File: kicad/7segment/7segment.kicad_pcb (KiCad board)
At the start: 2 copper layers, 49.5 x 30.5 mm, 11 parts, among them P1 CONN_01X05, U1 74HC595

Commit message: Add a nice logo
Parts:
- added G***: made by ami, led2layer:superme, F.Cu at (113.8, 102.1)
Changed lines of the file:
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@@
     (tracks 107)
     (zones 0)
-    (modules 11)
+    (modules 12)
     (nets 23)
   )
@@
     (pad_to_mask_clearance 0.2)
     (aux_axis_origin 0 0)
+    (grid_origin 105.156 73.914)
     (visible_elements 7FFFFFFF)
     (pcbplotparams
@@
     )
   )
+  (module led2layer:superme (layer F.Cu)
+    (at 113.792 102.108)
+    (fp_text reference G*** (at 0 0) (layer F.SilkS) hide
+      (effects (font (thickness 0.3)))
+    )
+    (fp_text value "made by ami" (at 11.938 1.524) (layer F.SilkS)
+      (effects (font (thickness 0.3)))
+    )
+    (fp_poly (pts (xy -1.174848 -1.001932) (xy -1.108553 -0.835263) (xy -1.101964 -0.783166) (xy -1.154454 -0.687075)
+      (xy -1.261268 -0.703585) (xy -1.307612 -0.754359) (xy -1.321651 -0.891512) (xy -1.300826 -0.973125)
+      (xy -1.241858 -1.063868) (xy -1.174848 -1.001932)) (layer F.SilkS) (width 0.01))
+    (fp_poly (pts (xy -1.354667 -0.635) (xy -1.397 -0.592666) (xy -1.439334 -0.635) (xy -1.397 -0.677333)
+      (xy -1.354667 -0.635)) (layer F.SilkS) (width 0.01))
+    (fp_poly (pts (xy -1.222468 -0.515682) (xy -1.213556 -0.461942) (xy -1.232025 -0.346905) (xy -1.293325 -0.393625)
+      (xy -1.308718 -0.417483) (xy -1.304455 -0.524221) (xy -1.285493 -0.540758) (xy -1.222468 -0.515682)) (layer F.SilkS) (width 0.01))
+    (fp_poly (pts (xy 0.599715 -2.134372) (xy 0.911081 -2.038929) (xy 1.037166 -1.989426) (xy 1.167461 -1.881387)
+      (xy 1.162036 -1.761872) (xy 1.029634 -1.692658) (xy 0.994833 -1.690333) (xy 0.868566 -1.682959)
+      (xy 0.880286 -1.647657) (xy 1.016 -1.566333) (xy 1.137143 -1.47808) (xy 1.103782 -1.442679)
+      (xy 1.095464 -1.442333) (xy 0.94105 -1.385676) (xy 0.776868 -1.26568) (xy 0.623349 -1.156396)
+      (xy 0.516497 -1.137748) (xy 0.409623 -1.120328) (xy 0.337892 -1.057401) (xy 0.276273 -0.955299)
+      (xy 0.288945 -0.931333) (xy 0.297454 -0.868359) (xy 0.24551 -0.740833) (xy 0.194676 -0.622351)
+      (xy 0.213574 -0.613099) (xy 0.325194 -0.619887) (xy 0.415543 -0.570765) (xy 0.505205 -0.50776)
+      (xy 0.476141 -0.560746) (xy 0.4515 -0.592907) (xy 0.398848 -0.731912) (xy 0.471792 -0.883059)
+      (xy 0.591547 -0.994178) (xy 0.669689 -0.941895) (xy 0.707091 -0.725624) (xy 0.707114 -0.725223)
+      (xy 0.75408 -0.563375) (xy 0.831881 -0.50806) (xy 0.913935 -0.581838) (xy 0.925563 -0.740833)
+      (xy 0.934117 -0.971933) (xy 0.970574 -1.121833) (xy 1.09131 -1.239379) (xy 1.260868 -1.266013)
+      (xy 1.394579 -1.189125) (xy 1.397 -1.185333) (xy 1.367024 -1.122551) (xy 1.232663 -1.100666)
+      (xy 1.071188 -1.071386) (xy 1.016 -1.013272) (xy 1.085663 -0.923804) (xy 1.239987 -0.84161)
+      (xy 1.396976 -0.803943) (xy 1.45309 -0.814692) (xy 1.487392 -0.774007) (xy 1.481946 -0.620595)
+      (xy 1.441314 -0.40516) (xy 1.404521 -0.275166) (xy 1.325172 -0.117043) (xy 1.219304 -0.110291)
+      (xy 1.059049 -0.253209) (xy 1.058333 -0.254) (xy 0.896313 -0.383263) (xy 0.75405 -0.420317)
+      (xy 0.679782 -0.355588) (xy 0.677333 -0.329608) (xy 0.615403 -0.273913) (xy 0.545935 -0.286305)
+      (xy 0.458536 -0.292222) (xy 0.466266 -0.25303) (xy 0.429348 -0.196794) (xy 0.25794 -0.170137)
+      (xy 0.211666 -0.169333) (xy 0.009146 -0.148731) (xy -0.044548 -0.090596) (xy -0.03927 -0.07971)
+      (xy 0.077479 -0.030202) (xy 0.259994 -0.04365) (xy 0.461311 -0.06376) (xy 0.600186 -0.038595)
+      (xy 0.644412 0.013937) (xy 0.561786 0.075929) (xy 0.507146 0.093778) (xy 0.381749 0.13362)
+      (xy 0.403153 0.152254) (xy 0.574157 0.160894) (xy 0.804189 0.128672) (xy 0.900715 0.042334)
+      (xy 0.991026 -0.075065) (xy 1.075142 -0.043102) (xy 1.100666 0.0743) (xy 1.047241 0.246943)
+      (xy 0.924174 0.370553) (xy 0.787281 0.393643) (xy 0.765708 0.383292) (xy 0.695404 0.40585)
+      (xy 0.677333 0.503003) (xy 0.643188 0.626095) (xy 0.510212 0.672918) (xy 0.402166 0.676812)
+      (xy 0.121918 0.635573) (xy -0.127 0.546757) (xy -0.353951 0.391646) (xy -0.576503 0.181687)
+      (xy -0.602339 0.151756) (xy -0.731681 -0.017739) (xy -0.780609 -0.157721) (xy -0.761236 -0.340022)
+      (xy -0.726476 -0.479778) (xy 0.197555 -0.479778) (xy 0.209177 -0.429443) (xy 0.254 -0.423333)
+      (xy 0.32369 -0.454311) (xy 0.310444 -0.479778) (xy 0.209964 -0.489911) (xy 0.197555 -0.479778)
+      (xy -0.726476 -0.479778) (xy -0.715968 -0.522022) (xy -0.660159 -0.792024) (xy -0.640938 -1.01317)
+      (xy -0.64793 -1.082036) (xy -0.62543 -1.204114) (xy -0.386331 -1.204114) (xy -0.381486 -1.186119)
+      (xy -0.270983 -1.135403) (xy -0.061435 -1.114251) (xy 0.001014 -1.115195) (xy 0.198078 -1.138974)
+      (xy 0.289154 -1.182671) (xy 0.287839 -1.199076) (xy 0.182833 -1.244031) (xy -0.02455 -1.268502)
+      (xy -0.094661 -1.27) (xy -0.305222 -1.252056) (xy -0.386331 -1.204114) (xy -0.62543 -1.204114)
+      (xy -0.623635 -1.21385) (xy -0.460956 -1.339383) (xy -0.382569 -1.379201) (xy -0.167508 -1.467551)
+      (xy -0.013347 -1.473249) (xy 0.165174 -1.399149) (xy 0.168093 -1.397641) (xy 0.35354 -1.329977)
+      (xy 0.459959 -1.345811) (xy 0.462091 -1.348881) (xy 0.436878 -1.434438) (xy 0.361062 -1.475443)
+      (xy 0.215341 -1.584564) (xy 0.170875 -1.651) (xy 0.508 -1.651) (xy 0.550333 -1.608666)
+      (xy 0.592666 -1.651) (xy 0.550333 -1.693333) (xy 0.508 -1.651) (xy 0.170875 -1.651)
+      (xy 0.112621 -1.738035) (xy 0.059154 -1.907252) (xy 0.121908 -2.017901) (xy 0.201843 -2.075683)
+      (xy 0.377058 -2.145203) (xy 0.599715 -2.134372)) (layer F.SilkS) (width 0.01))
+    (fp_poly (pts (xy -0.638427 0.696059) (xy -0.610657 0.710364) (xy -0.333584 0.806884) (xy -0.041216 0.846667)
+      (xy 0.165659 0.864221) (xy 0.244082 0.930096) (xy 0.246309 0.994834) (xy 0.262332 1.209076)
+      (xy 0.348042 1.354723) (xy 0.473778 1.382126) (xy 0.476974 1.380945) (xy 0.557863 1.379531)
+      (xy 0.562261 1.490911) (xy 0.544479 1.576791) (xy 0.458654 1.791871) (xy 0.354662 1.926167)
+      (xy 0.162109 1.999354) (xy -0.12816 2.025034) (xy -0.45155 2.003951) (xy -0.743462 1.936849)
+      (xy -0.804334 1.912802) (xy -1.037774 1.776617) (xy -1.27972 1.589056) (xy -1.312334 1.559029)
+      (xy -1.462258 1.403416) (xy -1.492103 1.322867) (xy -1.422145 1.288472) (xy -1.272339 1.190234)
+      (xy -1.230246 1.116392) (xy -1.144008 0.944686) (xy -1.028387 0.773864) (xy -0.914312 0.645319)
+      (xy -0.808973 0.623131) (xy -0.638427 0.696059)) (layer F.SilkS) (width 0.01))
+    (fp_poly (pts (xy -0.123116 2.973568) (xy -0.112531 3.02262) (xy -0.122531 3.040769) (xy -0.10438 3.132843)
+      (xy -0.064028 3.156069) (xy -0.075412 3.175931) (xy -0.220909 3.185308) (xy -0.359317 3.184467)
+      (xy -0.59383 3.168927) (xy -0.738789 3.140046) (xy -0.761484 3.122084) (xy -0.688705 3.071024)
+      (xy -0.511422 3.019125) (xy -0.497417 3.01625) (xy -0.242246 2.972044) (xy -0.123116 2.973568)) (layer F.SilkS) (width 0.01))
+    (fp_poly (pts (xy -1.100667 3.175) (xy -1.143 3.217334) (xy -1.185334 3.175) (xy -1.143 3.132667)
+      (xy -1.100667 3.175)) (layer F.SilkS) (width 0.01))
+    (fp_poly (pts (xy -1.439334 3.175) (xy -1.481667 3.217334) (xy -1.524 3.175) (xy -1.481667 3.132667)
+      (xy -1.439334 3.175)) (layer F.SilkS) (width 0.01))
+    (fp_poly (pts (xy 4.318 3.386667) (xy -0.014112 3.386667) (xy -0.85098 3.385848) (xy -1.632976 3.383496)
+      (xy -2.344464 3.37977) (xy -2.969807 3.374827) (xy -3.493371 3.368825) (xy -3.899518 3.361923)
+      (xy -4.172613 3.354279) (xy -4.297021 3.34605) (xy -4.302872 3.343316) (xy -4.211925 3.334447)
+      (xy -3.968661 3.326199) (xy -3.590095 3.318758) (xy -3.093242 3.312313) (xy -2.495118 3.307049)
+      (xy -1.812737 3.303156) (xy -1.063115 3.30082) (xy -0.388637 3.300199) (xy 3.482246 3.300432)
+      (xy 3.426447 3.124624) (xy 3.33836 2.921254) (xy 3.19991 2.674949) (xy 3.040775 2.430322)
+      (xy 2.890634 2.231989) (xy 2.779164 2.124563) (xy 2.755944 2.116667) (xy 2.615922 2.062118)
+      (xy 2.553992 2.012126) (xy 2.424906 1.938697) (xy 2.181789 1.842314) (xy 1.874531 1.742508)
+      (xy 1.838558 1.732044) (xy 1.527171 1.638355) (xy 1.346147 1.564754) (xy 1.262095 1.488226)
+      (xy 1.241621 1.385758) (xy 1.244432 1.322552) (xy 1.311817 1.119249) (xy 1.464825 0.873366)
+      (xy 1.556956 0.76123) (xy 1.75631 0.493924) (xy 1.914345 0.201321) (xy 1.955278 0.091535)
+      (xy 2.051101 -0.132736) (xy 2.165889 -0.277111) (xy 2.200698 -0.296132) (xy 2.379044 -0.439029)
+      (xy 2.538287 -0.746089) (xy 2.622211 -1.002439) (xy 2.656289 -1.272941) (xy 2.5907 -1.566551)
+      (xy 2.564276 -1.637439) (xy 2.402392 -1.96713) (xy 2.189727 -2.287811) (xy 1.962933 -2.551272)
+      (xy 1.758662 -2.709306) (xy 1.744278 -2.716) (xy 1.540879 -2.817728) (xy 1.439333 -2.878515)
+      (xy 1.264743 -2.970376) (xy 1.081117 -3.04534) (xy 0.91349 -3.145121) (xy 0.899675 -3.256956)
+      (xy 0.938361 -3.301971) (xy 1.029329 -3.335469) (xy 1.194012 -3.359052) (xy 1.453843 -3.374324)
+      (xy 1.830254 -3.382888) (xy 2.344679 -3.386348) (xy 2.633725 -3.386666) (xy 4.318 -3.386666)
+      (xy 4.318 3.386667)) (layer F.SilkS) (width 0.01))
+  )
   (gr_text "(C) Amitesh Singh 2017" (at 136.652 91.694 90) (layer B.SilkS)
     (effects (font (size 1.5 1.5) (thickness 0.3)) (justify mirror))
@@
     (effects (font (size 1.5 1.5) (thickness 0.3) italic))
   )
-  (gr_text V0.1 (at 113.284 104.14) (layer F.SilkS)
+  (gr_text V0.1 (at 154.178 78.486) (layer F.SilkS)
     (effects (font (size 1.5 1.5) (thickness 0.3)))
   )

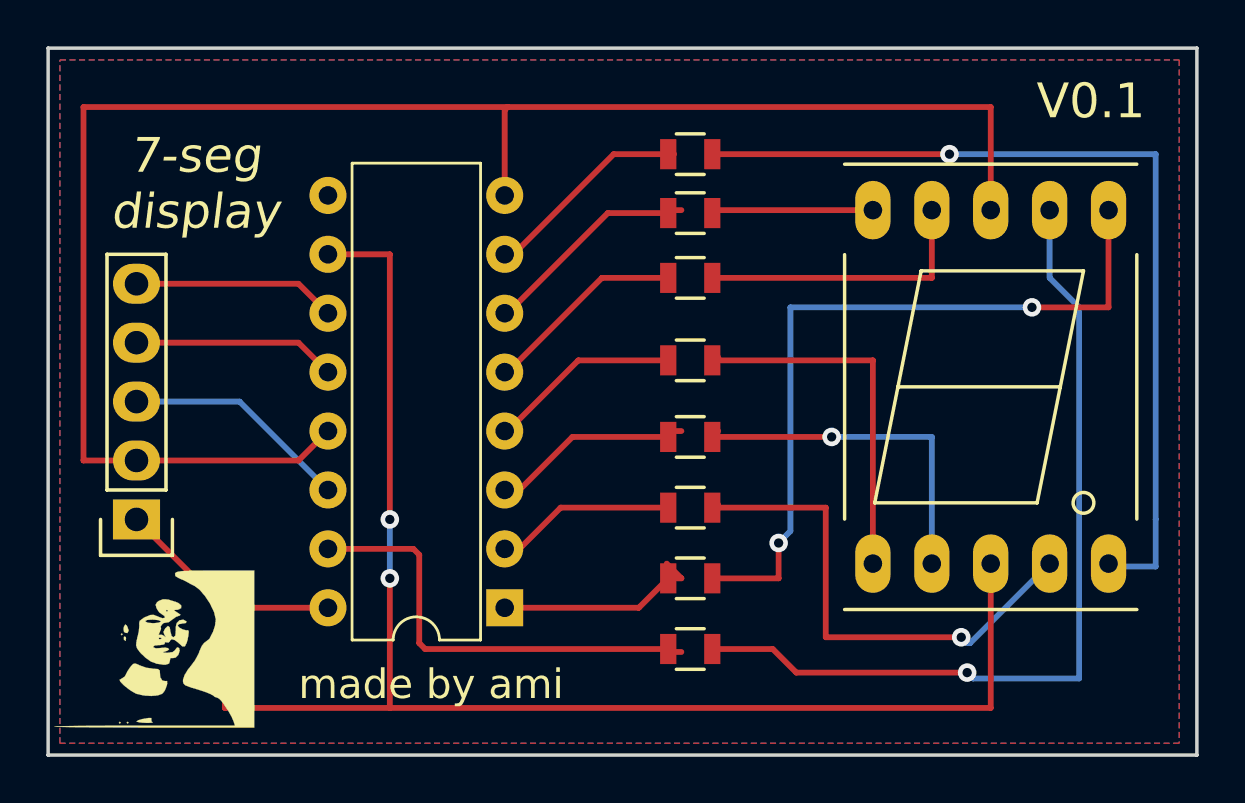
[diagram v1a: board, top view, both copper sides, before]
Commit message: update the 7segment a bit
mistakes corrected.

- remove right angled traces
- minimize the vias
- add a 2.0 mm hole

Signed-off-by: Amitesh Singh <singh.amitesh@gmail.com>
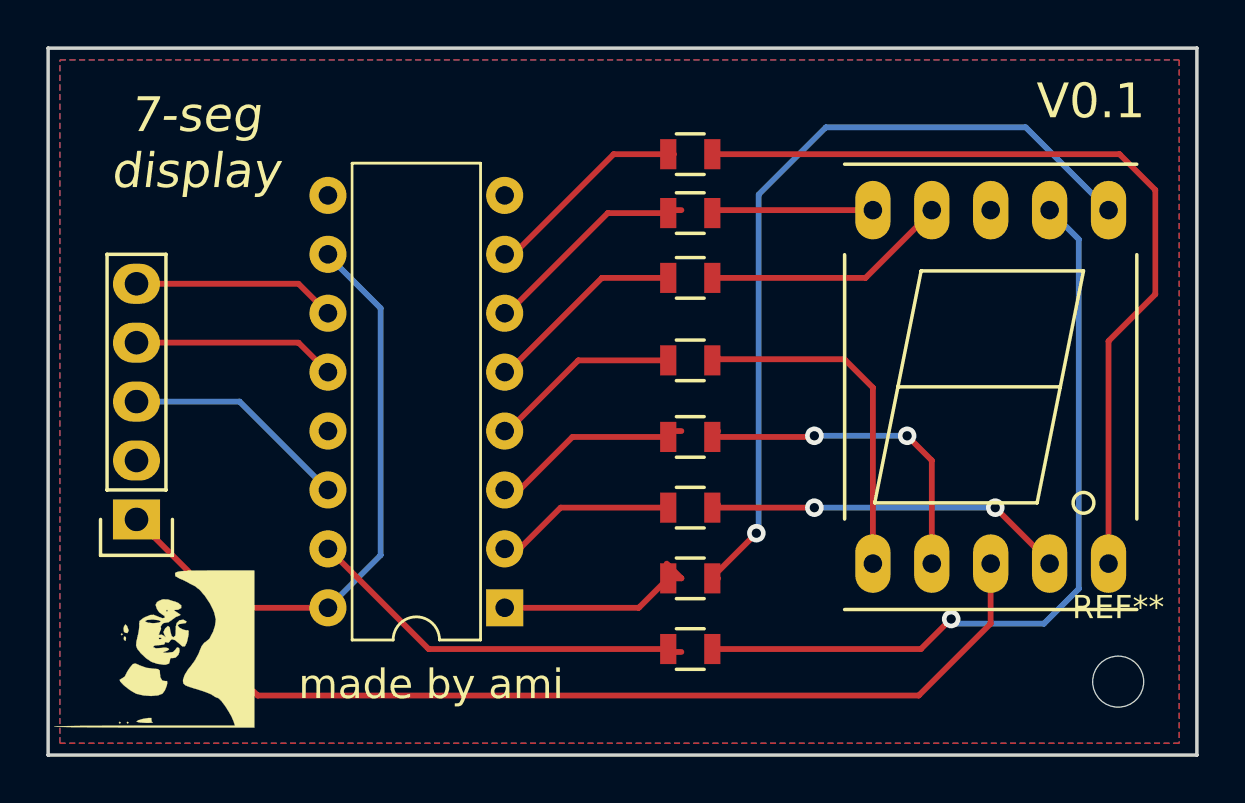
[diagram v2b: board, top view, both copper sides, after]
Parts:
- added REF**: M1, Mounting_Holes:MountingHole_2.2mm_M2, F.Cu at (155.4, 103.5)
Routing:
- net GND: track 73.7 -> 0.00 mm
- net VCC: track 75.6 -> 66.8 mm, vias 2 -> 0
- net Net-(R6-Pad2): track 22.6 -> 15.9 mm, vias 1 -> 2
- net Net-(R8-Pad2): track 37.1 -> 33.9 mm
- net Net-(R1-Pad2): track 39.4 -> 36.7 mm, vias 1 -> 0
- net Net-(R7-Pad2): track 33.0 -> 35.5 mm, vias 2 -> 1
- net /seg0: track 19.0 -> 16.8 mm
- net Net-(R3-Pad2): track 12.4 -> 10.7 mm
- net Net-(R4-Pad2): track 16.0 -> 15.4 mm
- net Net-(R5-Pad2): track 15.2 -> 14.7 mm, vias 1 -> 2
- added copper zone on F.Cu, net GND
- removed copper zone on F.Cu, net VCC
